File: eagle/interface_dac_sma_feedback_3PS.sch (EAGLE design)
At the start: 31 parts, among them IC1 ISO1540, T1 TIP122V, T2 TIP122V, T3 TIP122V, X1 BU-SMA-V

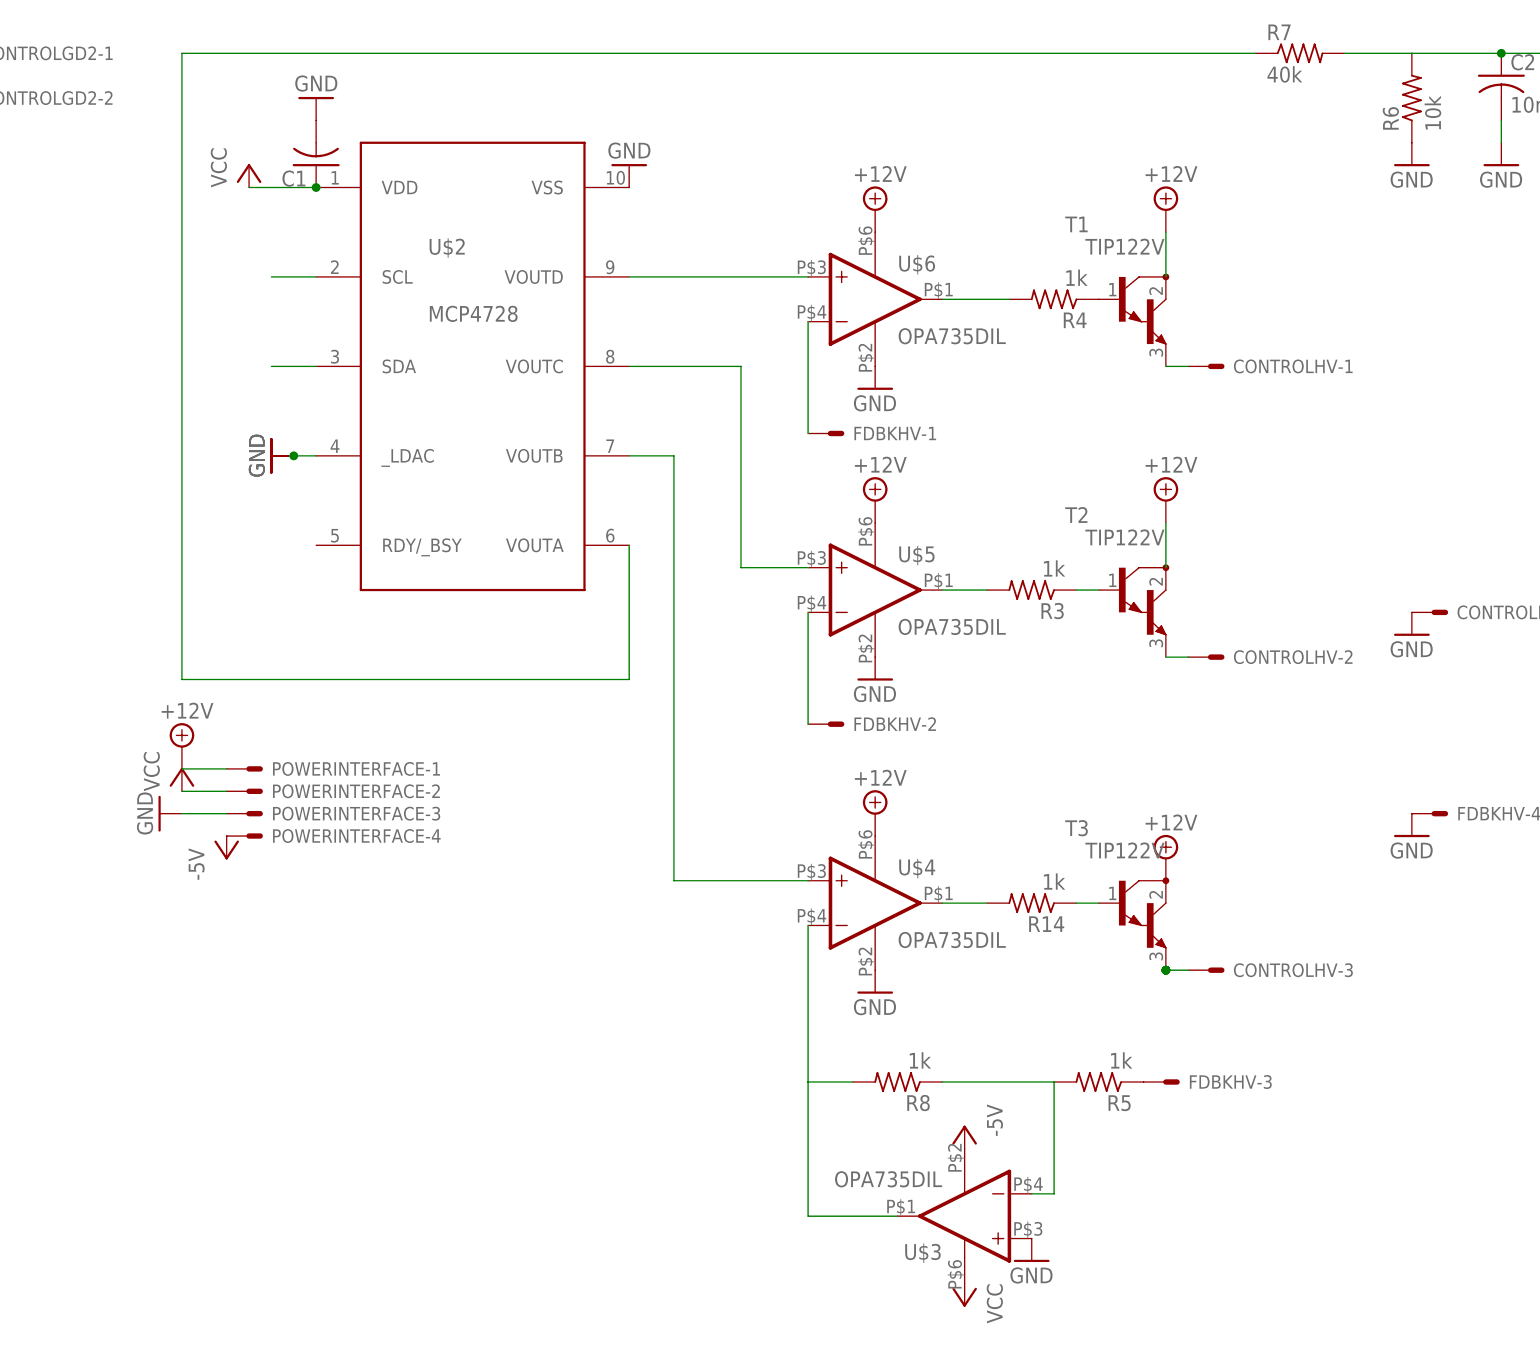
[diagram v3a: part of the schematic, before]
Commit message: use lt1352 opamp for feedback, smd output up to 1.6kVpp
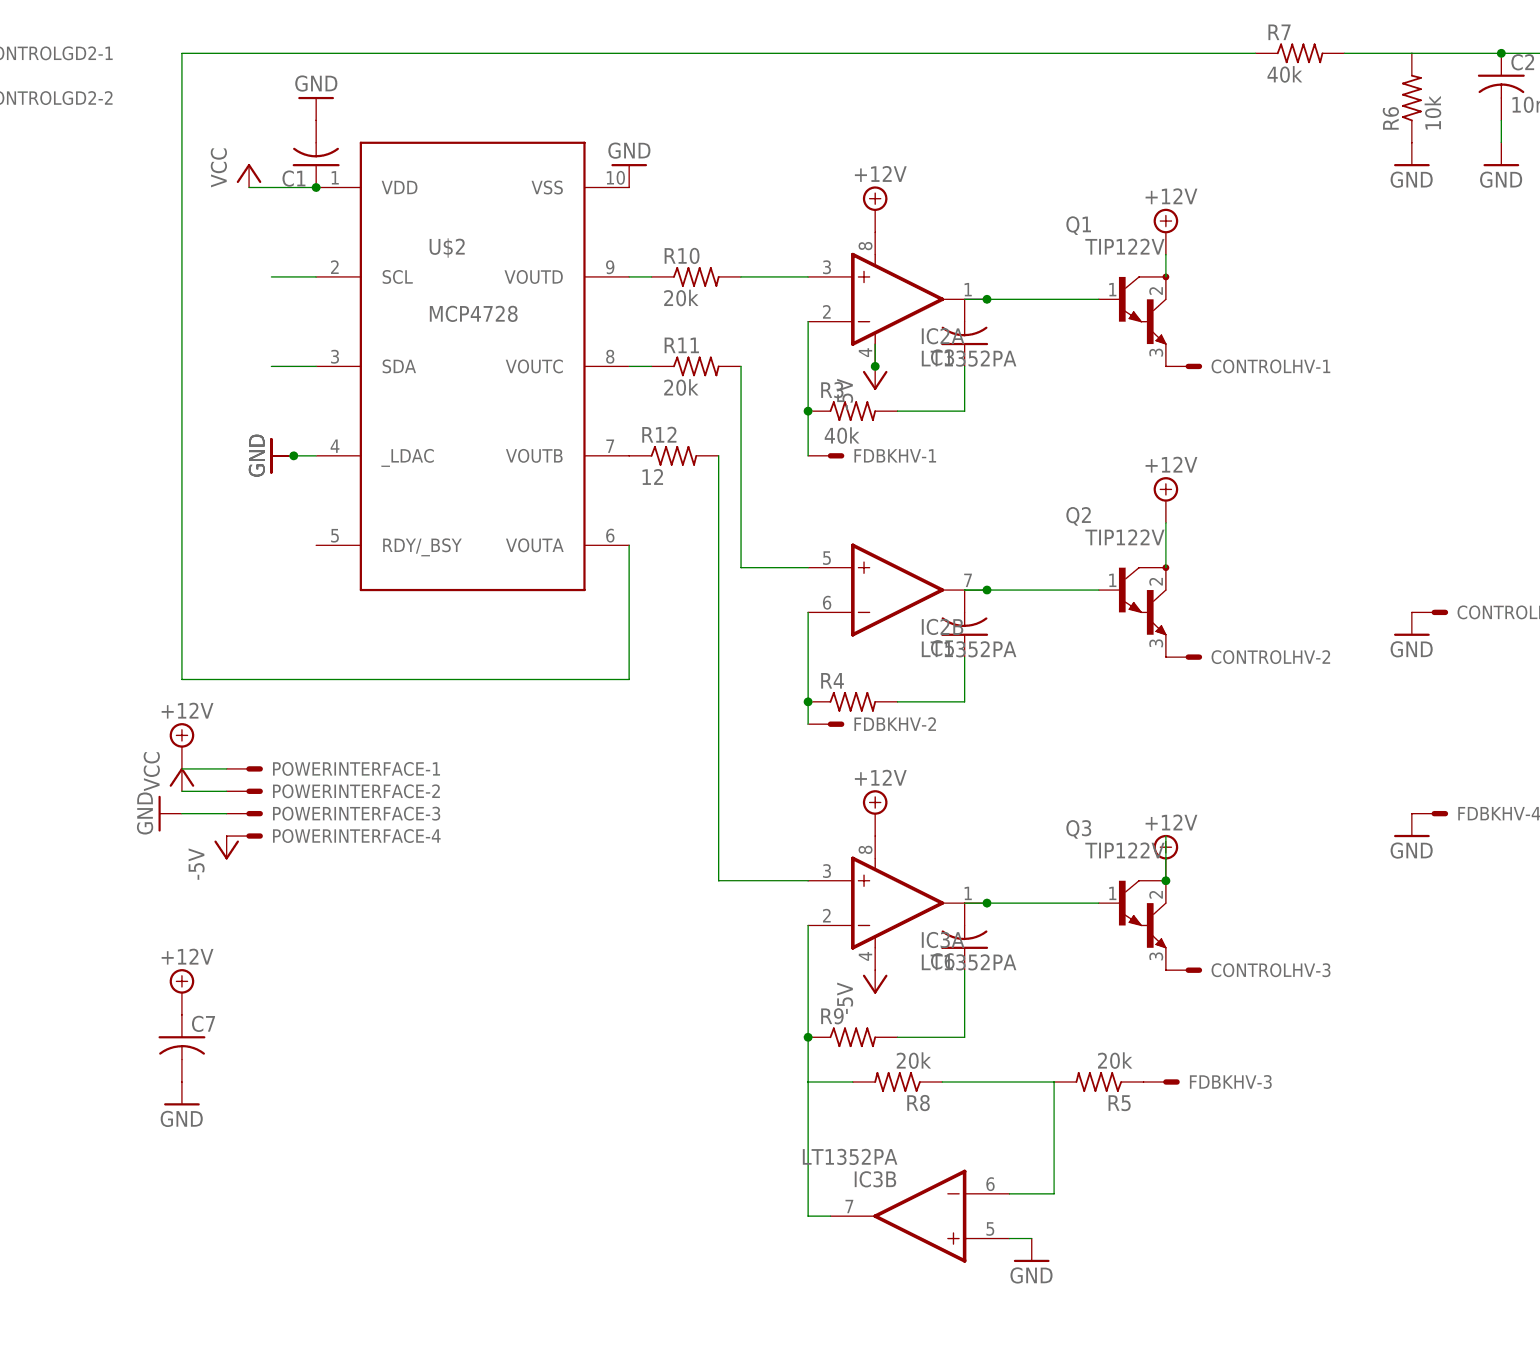
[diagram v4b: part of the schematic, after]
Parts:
- removed R14: 1k, resistor:R-US_0207/12
- removed U$3, U$4, U$5, U$6: OPA735DIL, texas:OPA735DIL
- added C3, C5, C6: (no value), resistor:C-US050-024X044
- added C7: (no value), resistor:C-US050-050X075
- added IC2, IC3: LT1352PA, linear-technology:LT1352PA
- added R10, R11: 20k, resistor:R-US_0207/12
- added R12: 12, resistor:R-US_0207/12
- added R9: (no value), resistor:R-US_0207/12
- FDBKHV: value (none) -> 40k
- R3, R4: value 1k -> (none)
- R5, R8: value 1k -> 20k
- renumbered T1 to Q1, T2 to Q2, T3 to Q3
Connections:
- new net N$24: R10.1, U$2.VOUTD
- new net N$25: R12.1, U$2.VOUTB
- new net N$26: R11.1, U$2.VOUTC
- net +12V: now also C7.1, IC2A.V+, IC3A.V+; no longer U$4.V+, U$5.V+, U$6.V+
- net -5V: now also IC2A.V-, IC3A.V-; no longer U$3.V-
- net GND: now also C7.2, IC3B.+IN; no longer U$3.+IN, U$4.V-, U$5.V-, U$6.V-
- net N$10: now also C5.2, IC2B.OUT, Q2.B; no longer R3.2, U$5.OUT
- net N$14: now also IC3A.-IN, IC3B.OUT, R9.1; no longer U$3.OUT, U$4.-IN
- net N$15: now also C5.1, R4.2; no longer Q3.B, R14.1
- net N$16: now also IC2A.+IN, R10.2; no longer U$2.VOUTD, U$6.+IN
- net N$17: now also IC2B.+IN, R11.2; no longer U$2.VOUTC, U$5.+IN
- net N$18: now also IC3A.+IN, R12.2; no longer U$2.VOUTB, U$4.+IN
- net N$19: now also C3.2, IC2A.OUT, Q1.B; no longer R4.2, U$6.OUT
- net N$20: now also C6.1, R9.2; no longer Q2.B, R3.1
- net N$21: now also C6.2, IC3A.OUT, Q3.B; no longer R14.2, U$4.OUT
- net N$23: now also IC3B.-IN; no longer U$3.-IN
- net N$3: now also C3.1, R3.2; no longer Q1.B, R4.1
- net N$6: now also IC2B.-IN, R4.1; no longer U$5.-IN
- net N$8: now also IC2A.-IN, R3.1; no longer U$6.-IN
- net VCC: no longer U$3.V+
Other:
- moved on the sheet: CONTROLHV-1, CONTROLHV-2, CONTROLHV-3, FDBKHV-1, R3, R4

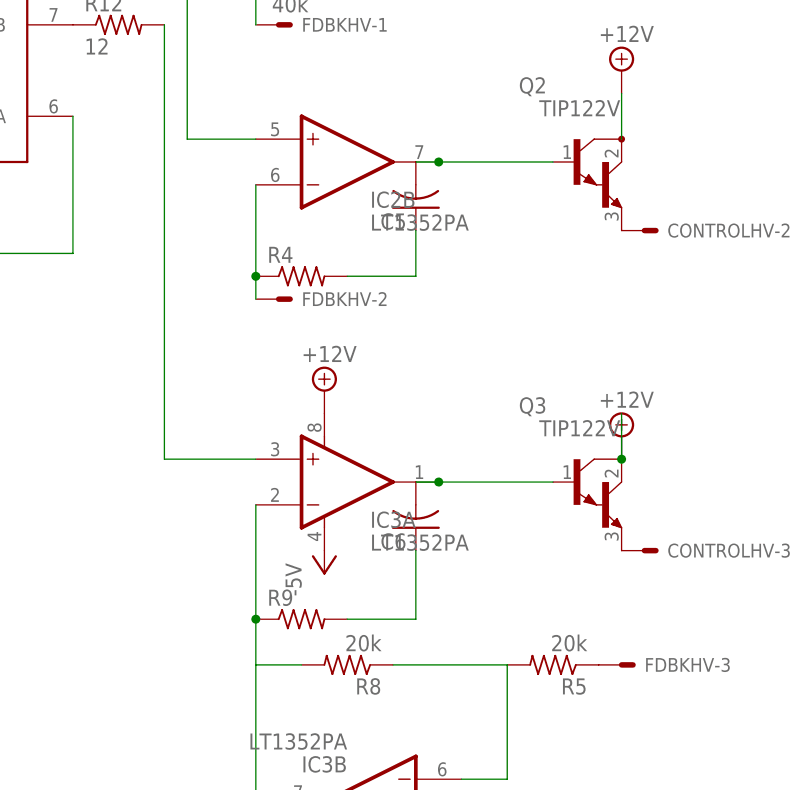
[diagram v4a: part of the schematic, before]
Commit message: more smd changes
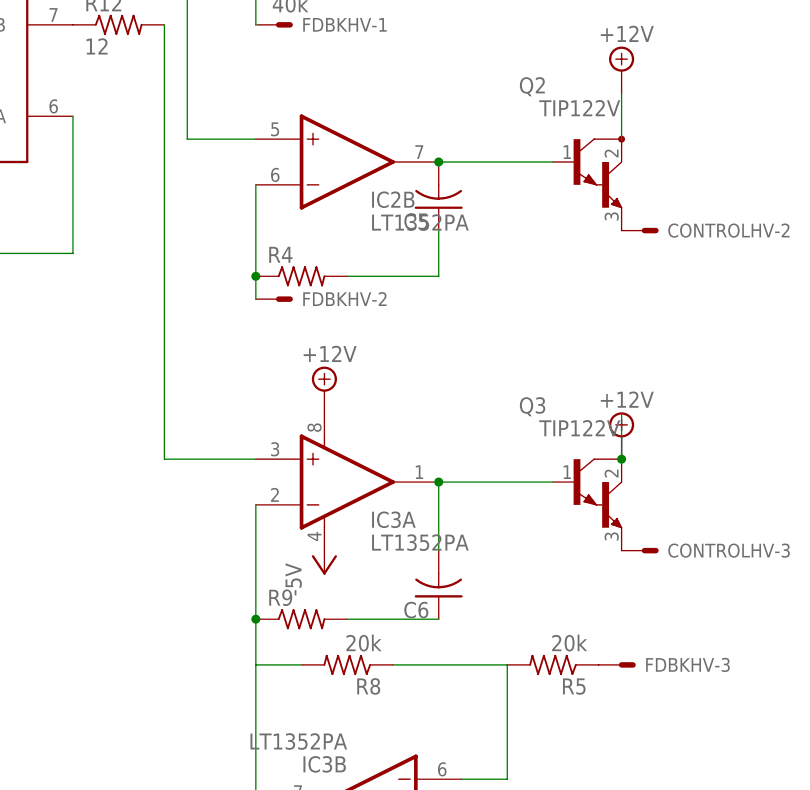
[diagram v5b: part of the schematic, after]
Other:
- moved on the sheet: C5, C6
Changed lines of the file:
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@@
 <instance part="C3" gate="G$1" x="177.8" y="86.36" rot="R180"/>
 <instance part="R4" gate="G$1" x="165.1" y="45.72"/>
-<instance part="C5" gate="G$1" x="177.8" y="53.34" rot="R180"/>
+<instance part="C5" gate="G$1" x="180.34" y="53.34" rot="R180"/>
 <instance part="R9" gate="G$1" x="165.1" y="7.62"/>
-<instance part="C6" gate="G$1" x="177.8" y="17.78" rot="R180"/>
+<instance part="C6" gate="G$1" x="180.34" y="10.16" rot="R180"/>
 <instance part="P+14" gate="+12V" x="88.9" y="12.7"/>
 <instance part="C7" gate="G$1" x="88.9" y="7.62"/>
@@
 <wire x1="193.04" y1="58.42" x2="180.34" y2="58.42" width="0.1524" layer="91"/>
 <pinref part="C5" gate="G$1" pin="2"/>
-<wire x1="180.34" y1="58.42" x2="177.8" y2="58.42" width="0.1524" layer="91"/>
 <pinref part="Q2" gate="G$1" pin="B"/>
 <pinref part="IC2" gate="B" pin="OUT"/>
@@
 <wire x1="193.04" y1="22.86" x2="180.34" y2="22.86" width="0.1524" layer="91"/>
 <pinref part="C6" gate="G$1" pin="2"/>
-<wire x1="180.34" y1="22.86" x2="177.8" y2="22.86" width="0.1524" layer="91"/>
+<wire x1="180.34" y1="22.86" x2="180.34" y2="15.24" width="0.1524" layer="91"/>
 <pinref part="Q3" gate="G$1" pin="B"/>
 <pinref part="IC3" gate="A" pin="OUT"/>
@@
 <pinref part="R4" gate="G$1" pin="2"/>
 <pinref part="C5" gate="G$1" pin="1"/>
-<wire x1="170.18" y1="45.72" x2="177.8" y2="45.72" width="0.1524" layer="91"/>
-<wire x1="177.8" y1="45.72" x2="177.8" y2="50.8" width="0.1524" layer="91"/>
+<wire x1="170.18" y1="45.72" x2="180.34" y2="45.72" width="0.1524" layer="91"/>
+<wire x1="180.34" y1="45.72" x2="180.34" y2="50.8" width="0.1524" layer="91"/>
 </segment>
 </net>
@@
 <pinref part="R9" gate="G$1" pin="2"/>
 <pinref part="C6" gate="G$1" pin="1"/>
-<wire x1="170.18" y1="7.62" x2="177.8" y2="7.62" width="0.1524" layer="91"/>
-<wire x1="177.8" y1="7.62" x2="177.8" y2="15.24" width="0.1524" layer="91"/>
-</segment>
-</net>
+<wire x1="170.18" y1="7.62" x2="180.34" y2="7.62" width="0.1524" layer="91"/>
+</segment>
+</net>
